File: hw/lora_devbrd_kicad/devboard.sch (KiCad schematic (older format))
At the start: 3 parts

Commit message: WIP: [kicad] adds peripherail connectors in schematics
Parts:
- added J?: Conn_01x05_MountingPin, symbol Connector_Generic_MountingPin:Conn_01x05_MountingPin
- added J? (x2): Conn_01x11_Male, symbol Connector:Conn_01x11_Male
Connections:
- net labels added: CTS, MISO, MOSI, NSS, PA0, PA10, PA15, PA3, PA8, PA9, PB3, PB4, PB5, PC13, RTS, RX, SCK, SCL, SDA, SWCLK, SWDIO, TX
- wire segments 9 -> 43
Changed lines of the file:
@@
 Wire Wire Line
 	4000 2650 4850 2650
+$Comp
+L power:GND #PWR?
+U 1 1 5DB97714
+P 7250 2950
+F 0 "#PWR?" H 7250 2700 50  0001 C CNN
+F 1 "GND" H 7255 2777 50  0000 C CNN
+F 2 "" H 7250 2950 50  0001 C CNN
+F 3 "" H 7250 2950 50  0001 C CNN
+	1    7250 2950
+	1    0    0    -1
+$EndComp
+Wire Wire Line
+	6200 2950 7250 2950
+Wire Wire Line
+	6200 2550 7250 2550
+Wire Wire Line
+	7250 2550 7250 2750
+Connection ~ 7250 2950
+Wire Wire Line
+	6200 2750 7250 2750
+Connection ~ 7250 2750
+Wire Wire Line
+	7250 2750 7250 2950
+$Comp
+L Connector_Generic_MountingPin:Conn_01x05_MountingPin J?
+U 1 1 5DB9A833
+P 6000 1200
+F 0 "J?" H 6088 1164 50  0000 L CNN
+F 1 "Conn_01x05_MountingPin" H 6088 1073 50  0000 L CNN
+F 2 "" H 6000 1200 50  0001 C CNN
+F 3 "~" H 6000 1200 50  0001 C CNN
+	1    6000 1200
+	1    0    0    -1
+$EndComp
+Text GLabel 5350 1000 0    50   Input ~ 0
++3.3V
+Text GLabel 5350 1100 0    50   Input ~ 0
+nRST
+Text GLabel 5350 1200 0    50   Input ~ 0
+SWDIO
+Text GLabel 5350 1300 0    50   Input ~ 0
+SWCLK
+Text GLabel 5350 1400 0    50   Input ~ 0
+GND
+Wire Wire Line
+	5350 1000 5800 1000
+Wire Wire Line
+	5350 1100 5800 1100
+Wire Wire Line
+	5350 1200 5800 1200
+Wire Wire Line
+	5350 1300 5800 1300
+Wire Wire Line
+	5350 1400 5800 1400
+Text GLabel 4400 3650 0    50   Input ~ 0
+SWDIO
+Text GLabel 4400 3750 0    50   Input ~ 0
+SWCLK
+Wire Wire Line
+	4400 3650 4850 3650
+Wire Wire Line
+	4400 3750 4850 3750
+Text GLabel 8750 1200 2    50   Input ~ 0
+PA8
+Text GLabel 8750 1300 2    50   Input ~ 0
+PA9
+Text GLabel 8750 1400 2    50   Input ~ 0
+PA10
+Text GLabel 8750 1500 2    50   Input ~ 0
+NSS
+Text GLabel 8750 1600 2    50   Input ~ 0
+SCK
+Text GLabel 8750 1700 2    50   Input ~ 0
+MISO
+Text GLabel 8750 1800 2    50   Input ~ 0
+MOSI
+Text GLabel 8750 1900 2    50   Input ~ 0
+CTS
+Text GLabel 8750 2000 2    50   Input ~ 0
+RTS
+Text GLabel 8750 2100 2    50   Input ~ 0
+SWDIO
+Text GLabel 8750 2200 2    50   Input ~ 0
+SWCLK
+Text GLabel 10150 2200 2    50   Input ~ 0
+PA15
+Text GLabel 10150 2100 2    50   Input ~ 0
+PB3
+Text GLabel 10150 2000 2    50   Input ~ 0
+PB4
+Text GLabel 10150 1900 2    50   Input ~ 0
+PA3
+Text GLabel 10150 1800 2    50   Input ~ 0
+PB5
+Text GLabel 10150 1700 2    50   Input ~ 0
+TX
+Text GLabel 10150 1600 2    50   Input ~ 0
+RX
+Text GLabel 10150 1200 2    50   Input ~ 0
+PA0
+Text GLabel 10150 1300 2    50   Input ~ 0
+PC13
+Text GLabel 10150 1400 2    50   Input ~ 0
+SDA
+Text GLabel 10150 1500 2    50   Input ~ 0
+SCL
+$Comp
+L Connector:Conn_01x11_Male J?
+U 1 1 5DBB1F8B
+P 8300 1700
+F 0 "J?" H 8408 2381 50  0000 C CNN
+F 1 "Conn_01x11_Male" H 8408 2290 50  0000 C CNN
+F 2 "" H 8300 1700 50  0001 C CNN
+F 3 "~" H 8300 1700 50  0001 C CNN
+	1    8300 1700
+	1    0    0    -1
+$EndComp
+$Comp
+L Connector:Conn_01x11_Male J?
+U 1 1 5DBB3C7F
+P 9700 1700
+F 0 "J?" H 9808 2381 50  0000 C CNN
+F 1 "Conn_01x11_Male" H 9808 2290 50  0000 C CNN
+F 2 "" H 9700 1700 50  0001 C CNN
+F 3 "~" H 9700 1700 50  0001 C CNN
+	1    9700 1700
+	1    0    0    -1
+$EndComp
+Wire Wire Line
+	8500 1200 8750 1200
+Wire Wire Line
+	8500 1300 8750 1300
+Wire Wire Line
+	8500 1400 8750 1400
+Wire Wire Line
+	8500 1500 8750 1500
+Wire Wire Line
+	8500 1600 8750 1600
+Wire Wire Line
+	8500 1700 8750 1700
+Wire Wire Line
+	8500 1800 8750 1800
+Wire Wire Line
+	8500 1900 8750 1900
+Wire Wire Line
+	8500 2000 8750 2000
+Wire Wire Line
+	8500 2100 8750 2100
+Wire Wire Line
+	8500 2200 8750 2200
+Wire Wire Line
+	9900 1200 10150 1200
+Wire Wire Line
+	9900 1300 10150 1300
+Wire Wire Line
+	9900 1400 10150 1400
+Wire Wire Line
+	9900 1500 10150 1500
+Wire Wire Line
+	9900 1600 10150 1600
+Wire Wire Line
+	9900 1700 10150 1700
+Wire Wire Line
+	9900 1800 10150 1800
+Wire Wire Line
+	9900 1900 10150 1900
+Wire Wire Line
+	9900 2000 10150 2000
+Wire Wire Line
+	9900 2100 10150 2100
+Wire Wire Line
+	9900 2200 10150 2200
 $EndSCHEMATC

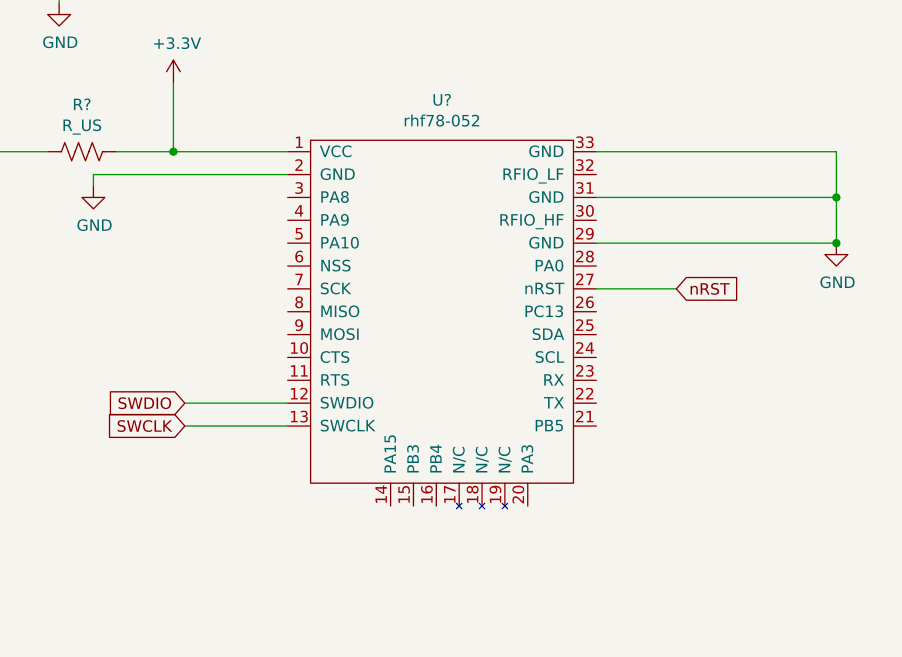
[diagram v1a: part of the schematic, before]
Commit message: WIP: [kicad] adds some network names to RHF78-052 pins
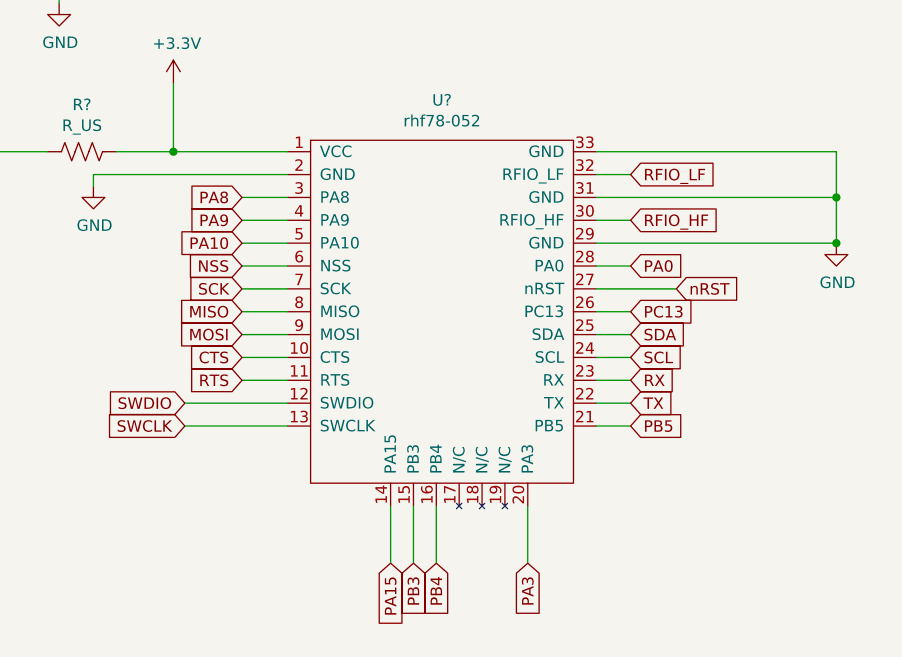
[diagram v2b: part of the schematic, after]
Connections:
- net labels added: RFIO_HF, RFIO_LF
- wire segments 43 -> 65
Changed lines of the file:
@@
 Wire Wire Line
 	9900 2200 10150 2200
+Text GLabel 4650 2750 0    50   Input ~ 0
+PA8
+Text GLabel 4650 2850 0    50   Input ~ 0
+PA9
+Text GLabel 4650 2950 0    50   Input ~ 0
+PA10
+Text GLabel 4650 3050 0    50   Input ~ 0
+NSS
+Text GLabel 4650 3150 0    50   Input ~ 0
+SCK
+Text GLabel 4650 3250 0    50   Input ~ 0
+MISO
+Text GLabel 4650 3350 0    50   Input ~ 0
+MOSI
+Text GLabel 4650 3450 0    50   Input ~ 0
+CTS
+Text GLabel 4650 3550 0    50   Input ~ 0
+RTS
+Text GLabel 6350 2650 2    50   Input ~ 0
+RFIO_LF
+Text GLabel 6350 2850 2    50   Input ~ 0
+RFIO_HF
+Text GLabel 6350 3050 2    50   Input ~ 0
+PA0
+Text GLabel 6350 3250 2    50   Input ~ 0
+PC13
+Text GLabel 6350 3350 2    50   Input ~ 0
+SDA
+Text GLabel 6350 3450 2    50   Input ~ 0
+SCL
+Text GLabel 6350 3550 2    50   Input ~ 0
+RX
+Text GLabel 6350 3650 2    50   Input ~ 0
+TX
+Text GLabel 6350 3750 2    50   Input ~ 0
+PB5
+Text GLabel 5900 4350 3    50   Input ~ 0
+PA3
+Text GLabel 5500 4350 3    50   Input ~ 0
+PB4
+Text GLabel 5400 4350 3    50   Input ~ 0
+PB3
+Text GLabel 5300 4350 3    50   Input ~ 0
+PA15
+Wire Wire Line
+	4650 2750 4850 2750
+Wire Wire Line
+	4650 2850 4850 2850
+Wire Wire Line
+	4650 2950 4850 2950
+Wire Wire Line
+	4650 3050 4850 3050
+Wire Wire Line
+	4650 3150 4850 3150
+Wire Wire Line
+	4650 3250 4850 3250
+Wire Wire Line
+	4650 3350 4850 3350
+Wire Wire Line
+	4650 3450 4850 3450
+Wire Wire Line
+	4650 3550 4850 3550
+Wire Wire Line
+	6200 2650 6350 2650
+Wire Wire Line
+	6200 2850 6350 2850
+Wire Wire Line
+	6200 3050 6350 3050
+Wire Wire Line
+	6200 3250 6350 3250
+Wire Wire Line
+	6200 3350 6350 3350
+Wire Wire Line
+	6200 3450 6350 3450
+Wire Wire Line
+	6200 3550 6350 3550
+Wire Wire Line
+	6200 3650 6350 3650
+Wire Wire Line
+	6200 3750 6350 3750
+Wire Wire Line
+	5900 4100 5900 4350
+Wire Wire Line
+	5500 4100 5500 4350
+Wire Wire Line
+	5400 4100 5400 4350
+Wire Wire Line
+	5300 4100 5300 4350
 $EndSCHEMATC

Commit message: WIP: [kicad] adds ft232rl and some indication led (pwr,rx,tx)
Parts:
- added C? (x3): C, symbol Device:C
- added D? (x3): LED, symbol Device:LED
- added J?: Conn_01x02_Male, symbol Connector:Conn_01x02_Male
- added R? (x3): R_US, symbol Device:R_US
- added U?: FT232RL, Package_SO:SSOP-28_5.3x10.2mm_P0.65mm, symbol Interface_USB:FT232RL
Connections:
- net labels added: D+, D-, RX_LED, TX_LED
- wire segments 65 -> 108
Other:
- moved on the sheet: C?, J?, R?, U?

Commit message: WIP: [kicad] adds usb connector, lm1117, custom indication leds, pwr and gnd connectors
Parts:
- added C2, C3: C, symbol Device:C
- added D? (x4): LED, symbol Device:LED
- added J4: USB_B_Micro, symbol Connector:USB_B_Micro
- added J? (x3): Conn_01x04_Female, symbol Connector:Conn_01x04_Female
- added R? (x4): R_US, symbol Device:R_US
- added U2: LM1117-3.3, symbol Regulator_Linear:LM1117-3.3
- gave numbers to parts that had none: 17
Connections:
- net labels added: +5V
- net labels removed: RFIO_HF, RFIO_LF
- wire segments 108 -> 168
- no-connect marks 0 -> 16
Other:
- moved on the sheet: D1, D2, D3, R2, R3, R4

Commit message: WIP: [kicad] ERC OK
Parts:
- removed J3: Conn_01x05_MountingPin, symbol Connector_Generic_MountingPin:Conn_01x05_MountingPin
- removed J? (x3): Conn_01x04_Female, symbol Connector:Conn_01x04_Female
- added J3, J5, J6: Conn_01x04_Male, symbol Connector:Conn_01x04_Male
- added SWD1: Conn_01x05_Male, symbol Connector:Conn_01x05_Male
- C1, C4, C6: value C -> 100nF
- C2, C3: value C -> 10uF
- C5: value C -> 4.7uF
- D3: value LED -> KP-2012EC
- D4, D5, D6, D7: renamed from D?; value LED -> KP-2012EC
- R1: value R_US -> 1K
- R2, R3, R4: value R_US -> 100
- R5, R6, R7, R8: renamed from R?; value R_US -> 100
- renumbered J5 to UART1
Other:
- moved on the sheet: C2, C3, D1, D2, D3, D4, D5, D6, D7, J4, R2, R3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

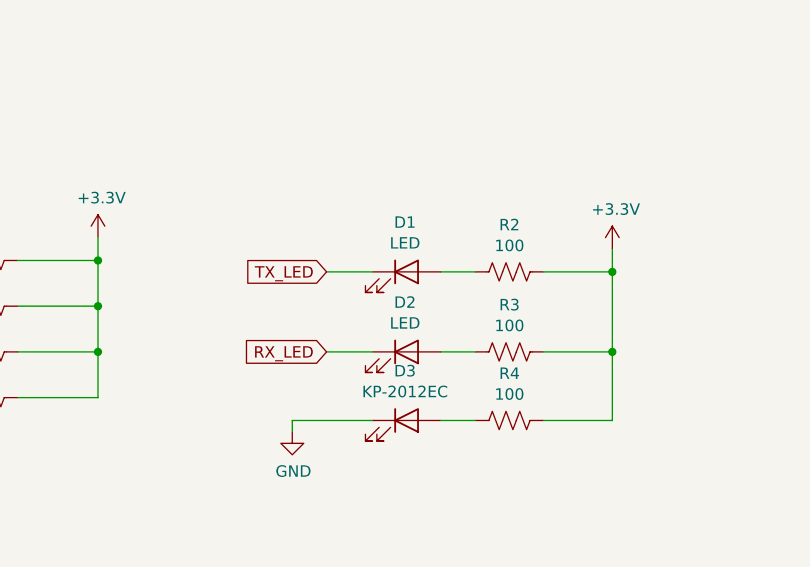
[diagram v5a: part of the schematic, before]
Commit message: WIP: [kicad] adds yellow and green leds for TX/RX indication
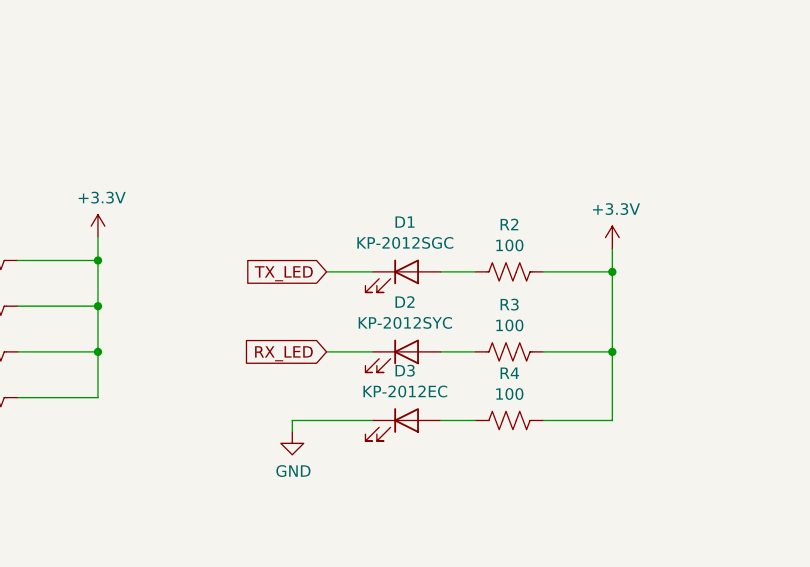
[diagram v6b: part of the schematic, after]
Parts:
- D1: value LED -> KP-2012SGC
- D2: value LED -> KP-2012SYC
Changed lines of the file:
@@
 EESchema Schematic File Version 4
+LIBS:devboard-cache
 EELAYER 26 0
 EELAYER END
@@
 P 5400 6050
 F 0 "D1" H 5393 6266 50  0000 C CNN
-F 1 "LED" H 5393 6175 50  0000 C CNN
+F 1 "KP-2012SGC" H 5393 6175 50  0000 C CNN
 F 2 "" H 5400 6050 50  0001 C CNN
 F 3 "~" H 5400 6050 50  0001 C CNN
@@
 P 5400 6400
 F 0 "D2" H 5393 6616 50  0000 C CNN
-F 1 "LED" H 5393 6525 50  0000 C CNN
+F 1 "KP-2012SYC" H 5393 6525 50  0000 C CNN
 F 2 "" H 5400 6400 50  0001 C CNN
 F 3 "~" H 5400 6400 50  0001 C CNN
